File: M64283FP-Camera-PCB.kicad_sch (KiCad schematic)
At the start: 7 parts, among them J1 JST_Connector, U1 M64283FP

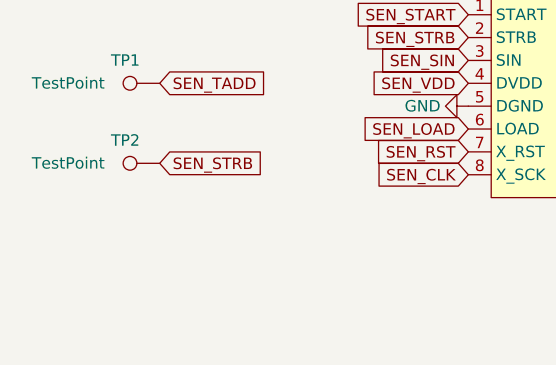
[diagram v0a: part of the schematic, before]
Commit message: Update project with new footprints and PCB shape
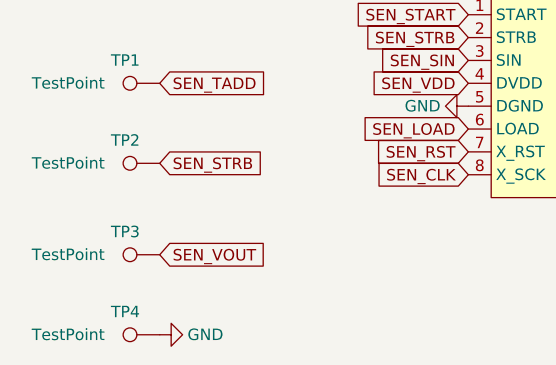
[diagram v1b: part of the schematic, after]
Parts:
- added TP3, TP4: TestPoint, TestPoint:TestPoint_Pad_1.5x1.5mm, symbol Connector:TestPoint
- C1, C2: footprint Capacitor_SMD:C_0603_1608Metric_Pad1.08x0.95mm_HandSolder -> SMT (LP):0603_HandSolder (LP)
- J1: footprint JST Connector:JST Connector -> JST Connector:JST Connector (LP)
- L1: footprint Inductor_SMD:L_1210_3225Metric_Pad1.42x2.65mm_HandSolder -> SMT (LP):1210_HandSolder (LP)
- U1: footprint M6428xFP:M6428xFP -> M6428xFP:M6428xFP (LP)
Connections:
- net GND: now also TP4.1
- net SEN_VOUT: now also TP3.1
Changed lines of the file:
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@@
+    )
+  )
+  (global_label "SEN_VOUT" (shape input) (at 81.28 137.16 0) (fields_autoplaced)
+    (effects (font (size 1.27 1.27)) (justify left))
+    (property "Intersheet References" "${INTERSHEET_REFS}" (id 0) (at 93.0669 137.0806 0)
+      (effects (font (size 1.27 1.27)) (justify left) hide)
     )
   )
@@
     (property "Reference" "L1" (id 0) (at 133.35 74.93 0))
     (property "Value" "220uH" (id 1) (at 133.35 77.47 0))
-    (property "Footprint" "Inductor_SMD:L_1210_3225Metric_Pad1.42x2.65mm_HandSolder" (id 2) (at 133.35 81.28 0)
+    (property "Footprint" "SMT (LP):1210_HandSolder (LP)" (id 2) (at 133.35 81.28 0)
       (effects (font (size 1.27 1.27)) hide)
     )
@@
     (pin "1")
     (pin "2")
+  )
+  (symbol (lib_id "Connector:TestPoint") (at 81.28 137.16 90) (unit 1)
+    (in_bom yes) (on_board yes)
+    (property "Reference" "TP3" (id 0) (at 77.47 134.62 90))
+    (property "Value" "TestPoint" (id 1) (at 71.12 137.16 90))
+    (property "Footprint" "TestPoint:TestPoint_Pad_1.5x1.5mm" (id 2) (at 81.28 132.08 0)
+      (effects (font (size 1.27 1.27)) hide)
+    )
+    (property "Datasheet" "~" (id 3) (at 81.28 132.08 0)
+      (effects (font (size 1.27 1.27)) hide)
+    )
+    (pin "1")
   )
   (symbol (lib_id "power:+5V") (at 121.92 81.28 90) (unit 1)
@@
       (effects (font (size 1.27 1.27)) (justify left))
     )
-    (property "Footprint" "Capacitor_SMD:C_0603_1608Metric_Pad1.08x0.95mm_HandSolder" (id 2) (at 142.24 87.63 0)
+    (property "Footprint" "SMT (LP):0603_HandSolder (LP)" (id 2) (at 142.24 87.63 0)
       (effects (font (size 1.27 1.27)) hide)
     )
@@
     (property "Reference" "J1" (id 0) (at 78.74 76.2 90))
     (property "Value" "JST_Connector" (id 1) (at 78.74 78.74 90))
-    (property "Footprint" "JST Connector:JST Connector" (id 2) (at 78.74 91.44 0)
+    (property "Footprint" "JST Connector:JST Connector (LP)" (id 2) (at 78.74 91.44 0)
       (effects (font (size 1.27 1.27)) hide)
     )
@@
     (pin "1")
   )
+  (symbol (lib_id "Connector:TestPoint") (at 81.28 146.05 90) (unit 1)
+    (in_bom yes) (on_board yes)
+    (property "Reference" "TP4" (id 0) (at 77.47 143.51 90))
+    (property "Value" "TestPoint" (id 1) (at 71.12 146.05 90))
+    (property "Footprint" "TestPoint:TestPoint_Pad_1.5x1.5mm" (id 2) (at 81.28 140.97 0)
+      (effects (font (size 1.27 1.27)) hide)
+    )
+    (property "Datasheet" "~" (id 3) (at 81.28 140.97 0)
+      (effects (font (size 1.27 1.27)) hide)
+    )
+    (pin "1")
+  )
   (symbol (lib_id "power:GND") (at 142.24 90.17 0) (unit 1)
     (in_bom yes) (on_board yes)
@@
     (pin "1")
   )
+  (symbol (lib_id "power:GND") (at 81.28 146.05 90) (unit 1)
+    (in_bom yes) (on_board yes)
+    (property "Reference" "#PWR01" (id 0) (at 87.63 146.05 0)
+      (effects (font (size 1.27 1.27)) hide)
+    )
+    (property "Value" "GND" (id 1) (at 86.36 146.05 90))
+    (property "Footprint" "" (id 2) (at 81.28 146.05 0)
+      (effects (font (size 1.27 1.27)) hide)
+    )
+    (property "Datasheet" "" (id 3) (at 81.28 146.05 0)
+      (effects (font (size 1.27 1.27)) hide)
+    )
+    (pin "1")
+  )
   (symbol (lib_id "power:+5V") (at 82.55 101.6 270) (unit 1)
     (in_bom yes) (on_board yes)
@@
       (effects (font (size 1.27 1.27)) (justify left))
     )
-    (property "Footprint" "Capacitor_SMD:C_0603_1608Metric_Pad1.08x0.95mm_HandSolder" (id 2) (at 124.46 87.63 0)
+    (property "Footprint" "SMT (LP):0603_HandSolder (LP)" (id 2) (at 124.46 87.63 0)
       (effects (font (size 1.27 1.27)) hide)
     )
@@
     (property "Reference" "U1" (id 0) (at 133.35 102.87 0))
     (property "Value" "M64283FP" (id 1) (at 133.35 105.41 0))
-    (property "Footprint" "M6428xFP:M6428xFP" (id 2) (at 133.35 119.38 0)
+    (property "Footprint" "M6428xFP:M6428xFP (LP)" (id 2) (at 133.35 119.38 0)
       (effects (font (size 1.27 1.27)) hide)
     )
@@
   )
   (symbol_instances
+    (path "/6f84667d-268b-48f9-bf73-f2997f0d6094"
+      (reference "#PWR01") (unit 1) (value "GND") (footprint "")
+    )
     (path "/ba61538f-c415-487f-8379-36ac61bc7348"
       (reference "#PWR02") (unit 1) (value "GND") (footprint "")
@@
     )
     (path "/832be189-bf5f-4b27-a169-79787db1f7b6"
-      (reference "C1") (unit 1) (value "0.15uF") (footprint "Capacitor_SMD:C_0603_1608Metric_Pad1.08x0.95mm_HandSolder")
+      (reference "C1") (unit 1) (value "0.15uF") (footprint "SMT (LP):0603_HandSolder (LP)")
     )
     (path "/24d9d241-6b46-4882-8dde-8b65afd74e4e"
-      (reference "C2") (unit 1) (value "0.15uF") (footprint "Capacitor_SMD:C_0603_1608Metric_Pad1.08x0.95mm_HandSolder")
+      (reference "C2") (unit 1) (value "0.15uF") (footprint "SMT (LP):0603_HandSolder (LP)")
     )
     (path "/339712eb-1f19-4124-bc10-71155b294b17"
-      (reference "J1") (unit 1) (value "JST_Connector") (footprint "JST Connector:JST Connector")
+      (reference "J1") (unit 1) (value "JST_Connector") (footprint "JST Connector:JST Connector (LP)")
     )
     (path "/027ca80f-d1b4-4fb1-a7bd-4cb44b4364c5"
-      (reference "L1") (unit 1) (value "220uH") (footprint "Inductor_SMD:L_1210_3225Metric_Pad1.42x2.65mm_HandSolder")
+      (reference "L1") (unit 1) (value "220uH") (footprint "SMT (LP):1210_HandSolder (LP)")
     )
     (path "/eb6bf613-f884-4cd1-a3e3-3044412a5db8"
@@
       (reference "TP2") (unit 1) (value "TestPoint") (footprint "TestPoint:TestPoint_Pad_1.5x1.5mm")
     )
+    (path "/0c811138-9bdf-4527-bde2-74eafdb82c77"
+      (reference "TP3") (unit 1) (value "TestPoint") (footprint "TestPoint:TestPoint_Pad_1.5x1.5mm")
+    )
+    (path "/57e1732b-7b92-4e48-b465-e743a235d686"
+      (reference "TP4") (unit 1) (value "TestPoint") (footprint "TestPoint:TestPoint_Pad_1.5x1.5mm")
+    )
     (path "/cdbf1ee1-a632-4796-b5a2-f148b7b0fa6f"
-      (reference "U1") (unit 1) (value "M64283FP") (footprint "M6428xFP:M6428xFP")
-    )
-  )
+      (reference "U1") (unit 1) (value "M64283FP") (footprint "M6428xFP:M6428xFP (LP)")
+    )
+  )

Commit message: Add Lightproof testpoint
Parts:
- TP1, TP2, TP3, TP4: footprint TestPoint:TestPoint_Pad_1.5x1.5mm -> SMT (LP):TestPoint_Pad_1.5x1.5mm (LP)
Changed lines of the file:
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@@
     (property "Reference" "TP3" (id 0) (at 77.47 134.62 90))
     (property "Value" "TestPoint" (id 1) (at 71.12 137.16 90))
-    (property "Footprint" "TestPoint:TestPoint_Pad_1.5x1.5mm" (id 2) (at 81.28 132.08 0)
+    (property "Footprint" "SMT (LP):TestPoint_Pad_1.5x1.5mm (LP)" (id 2) (at 81.28 132.08 0)
       (effects (font (size 1.27 1.27)) hide)
     )
@@
     (property "Reference" "TP2" (id 0) (at 77.47 124.46 90))
     (property "Value" "TestPoint" (id 1) (at 71.12 127 90))
-    (property "Footprint" "TestPoint:TestPoint_Pad_1.5x1.5mm" (id 2) (at 81.28 121.92 0)
+    (property "Footprint" "SMT (LP):TestPoint_Pad_1.5x1.5mm (LP)" (id 2) (at 81.28 121.92 0)
       (effects (font (size 1.27 1.27)) hide)
     )
@@
     (property "Reference" "TP4" (id 0) (at 77.47 143.51 90))
     (property "Value" "TestPoint" (id 1) (at 71.12 146.05 90))
-    (property "Footprint" "TestPoint:TestPoint_Pad_1.5x1.5mm" (id 2) (at 81.28 140.97 0)
+    (property "Footprint" "SMT (LP):TestPoint_Pad_1.5x1.5mm (LP)" (id 2) (at 81.28 140.97 0)
       (effects (font (size 1.27 1.27)) hide)
     )
@@
     (property "Reference" "TP1" (id 0) (at 77.47 115.57 90))
     (property "Value" "TestPoint" (id 1) (at 71.12 118.11 90))
-    (property "Footprint" "TestPoint:TestPoint_Pad_1.5x1.5mm" (id 2) (at 81.28 113.03 0)
+    (property "Footprint" "SMT (LP):TestPoint_Pad_1.5x1.5mm (LP)" (id 2) (at 81.28 113.03 0)
       (effects (font (size 1.27 1.27)) hide)
     )
@@
     )
     (path "/eb6bf613-f884-4cd1-a3e3-3044412a5db8"
-      (reference "TP1") (unit 1) (value "TestPoint") (footprint "TestPoint:TestPoint_Pad_1.5x1.5mm")
+      (reference "TP1") (unit 1) (value "TestPoint") (footprint "SMT (LP):TestPoint_Pad_1.5x1.5mm (LP)")
     )
     (path "/1fbaa233-4627-485f-95d8-d07b90aa6d36"
-      (reference "TP2") (unit 1) (value "TestPoint") (footprint "TestPoint:TestPoint_Pad_1.5x1.5mm")
+      (reference "TP2") (unit 1) (value "TestPoint") (footprint "SMT (LP):TestPoint_Pad_1.5x1.5mm (LP)")
     )
     (path "/0c811138-9bdf-4527-bde2-74eafdb82c77"
-      (reference "TP3") (unit 1) (value "TestPoint") (footprint "TestPoint:TestPoint_Pad_1.5x1.5mm")
+      (reference "TP3") (unit 1) (value "TestPoint") (footprint "SMT (LP):TestPoint_Pad_1.5x1.5mm (LP)")
     )
     (path "/57e1732b-7b92-4e48-b465-e743a235d686"
-      (reference "TP4") (unit 1) (value "TestPoint") (footprint "TestPoint:TestPoint_Pad_1.5x1.5mm")
+      (reference "TP4") (unit 1) (value "TestPoint") (footprint "SMT (LP):TestPoint_Pad_1.5x1.5mm (LP)")
     )
     (path "/cdbf1ee1-a632-4796-b5a2-f148b7b0fa6f"
